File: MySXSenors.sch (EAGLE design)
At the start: 6 parts

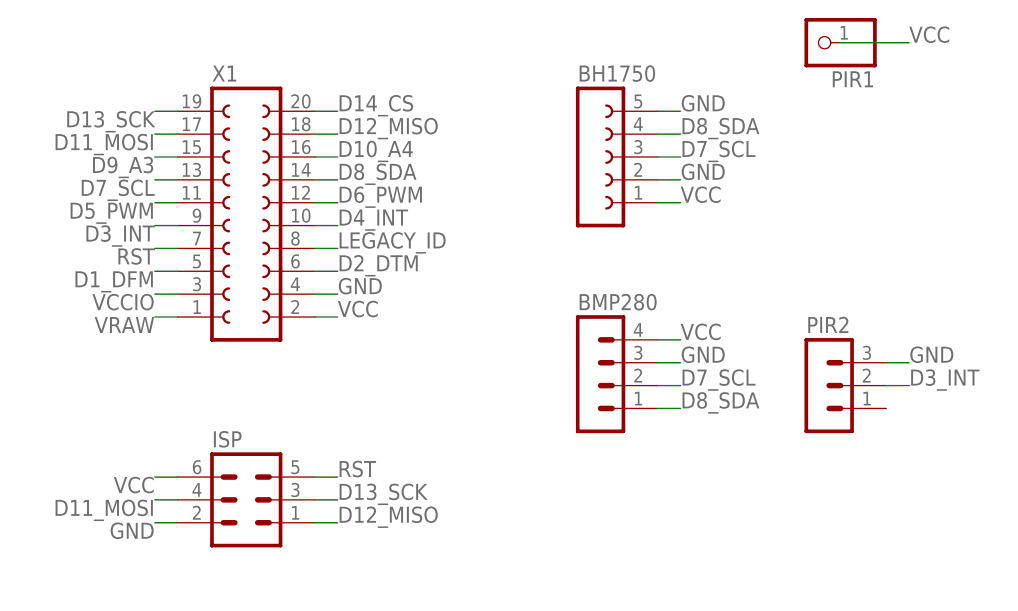
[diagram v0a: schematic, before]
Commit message: add uart
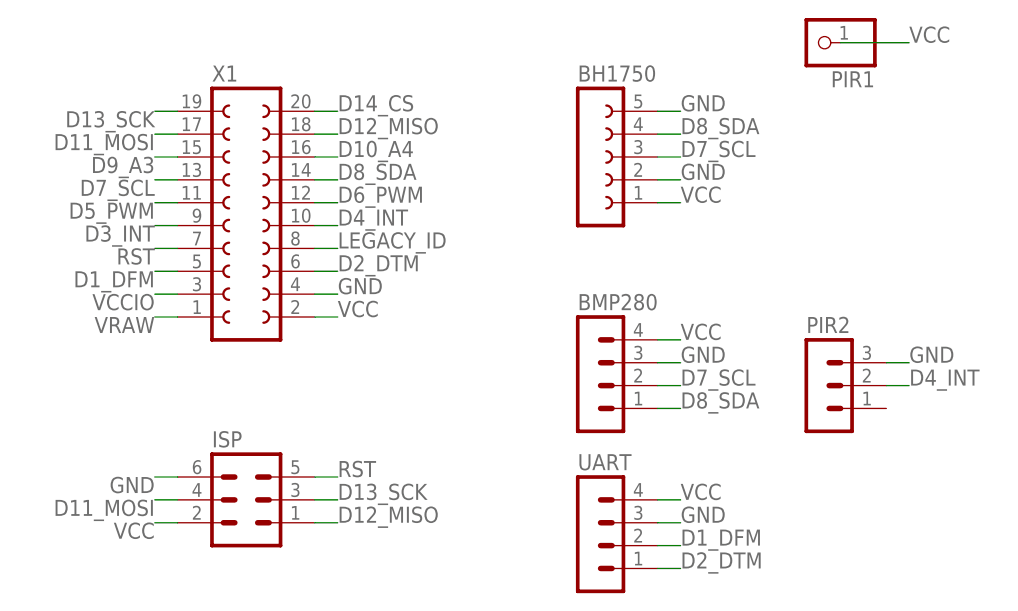
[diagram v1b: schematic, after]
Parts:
- added UART: (no value), con-lstb:MA04-1
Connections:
- net D1_DFM: now also UART.2
- net D2_DTM: now also UART.1
- net D3_INT: no longer PIR2.2
- net D4_INT: now also PIR2.2
- net GND: now also ISP.6, UART.3; no longer ISP.2
- net VCC: now also ISP.2, UART.4; no longer ISP.6

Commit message: make MysX connector smd mounted
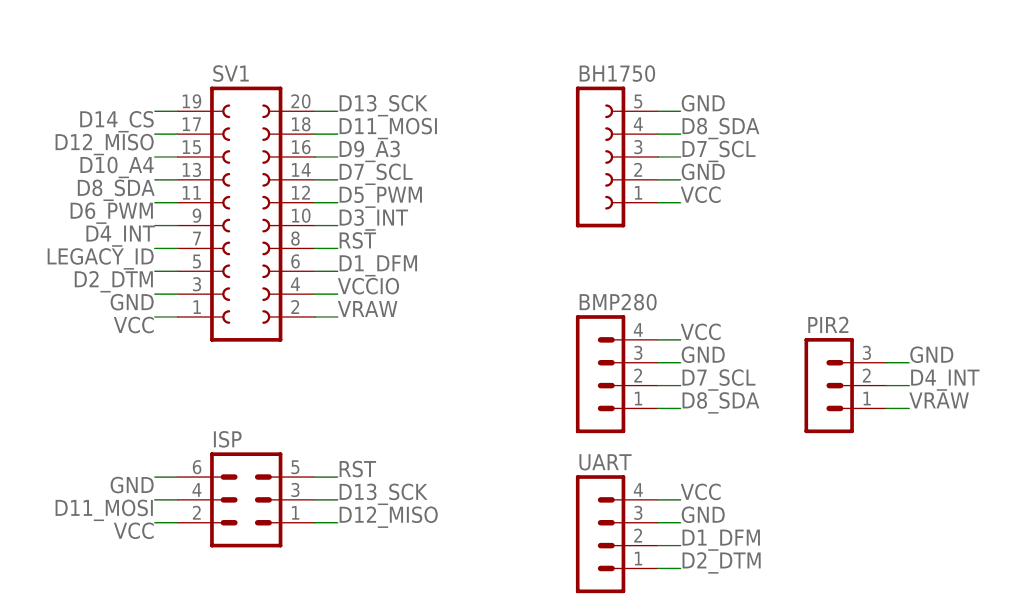
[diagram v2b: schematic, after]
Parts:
- removed PIR1: (no value), pinhead:PINHD-1X1
- removed X1: (no value), con-lsta:FE10-2
- added SV1: (no value), my-con-lsta:FE10-2
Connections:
- net D10_A4: now also SV1.15; no longer X1.16
- net D11_MOSI: now also SV1.18; no longer X1.17
- net D12_MISO: now also SV1.17; no longer X1.18
- net D13_SCK: now also SV1.20; no longer X1.19
- net D14_CS: now also SV1.19; no longer X1.20
- net D1_DFM: now also SV1.6; no longer X1.5
- net D2_DTM: now also SV1.5; no longer X1.6
- net D3_INT: now also SV1.10; no longer X1.9
- net D4_INT: now also SV1.9; no longer X1.10
- net D5_PWM: now also SV1.12; no longer X1.11
- net D6_PWM: now also SV1.11; no longer X1.12
- net D7_SCL: now also SV1.14; no longer X1.13
- net D8_SDA: now also SV1.13; no longer X1.14
- net D9_A3: now also SV1.16; no longer X1.15
- net GND: now also SV1.3; no longer X1.4
- net LEGACY_ID: now also SV1.7; no longer X1.8
- net RST: now also SV1.8; no longer X1.7
- net VCC: now also SV1.1; no longer PIR1.1, X1.2
- net VCCIO: now also SV1.4; no longer X1.3
- net VRAW: now also PIR2.1, SV1.2; no longer X1.1

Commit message: rename DTM and DTF signals
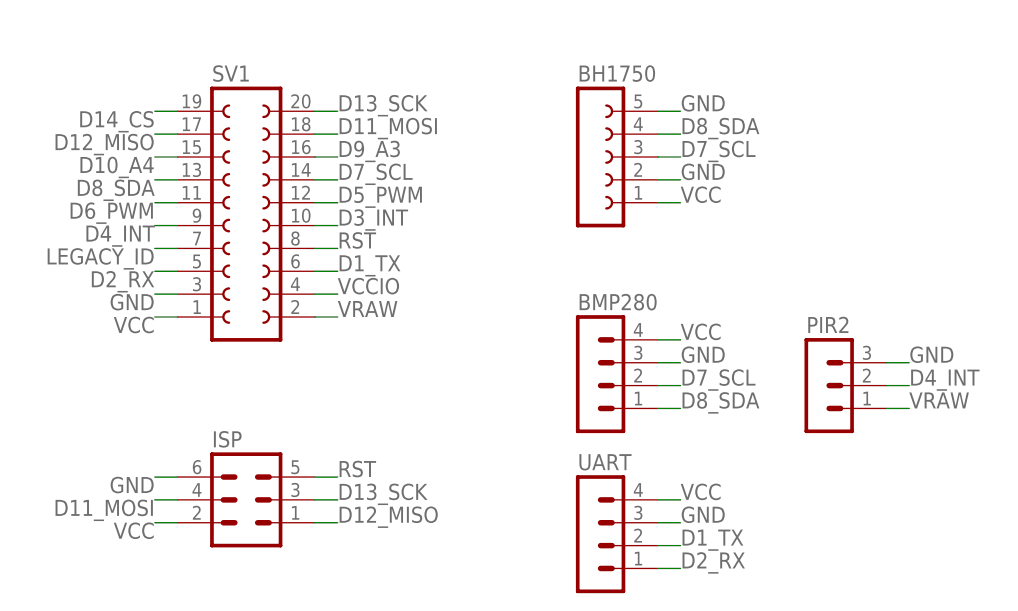
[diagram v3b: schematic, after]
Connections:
- net D1_DFM renamed D1_TX
- net D2_DTM renamed D2_RX
